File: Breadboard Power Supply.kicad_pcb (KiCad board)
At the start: 2 copper layers, 53.6 x 25.8 mm, 25 parts, among them J1 USB-C, J10 Conn_01x02_Male, J11 Conn_01x02_Male, J2 Conn_02x03_Odd_Even, J3 Conn_02x03_Odd_Even, J8 Conn_01x02_Male, J9 Conn_01x02_Male, U1 LM1117-1.8, U2 LM1117-3.3

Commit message: Layout tweaks.
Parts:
- moved R3 6.83 mm to (115.7, 75.9)
- moved R2 5.83 mm to (140.0, 76.2), turned to 0 degrees
- moved R1 1.63 mm to (136.9, 76.2), turned to 0 degrees
- moved C3 1.62 mm to (144.8, 80.6), turned to 90 degrees
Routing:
- net Net-(D1-K): track 5.49 -> 0.00 mm
- net Net-(J1-CC1): track 7.59 -> 12.9 mm
- net GND: track 23.8 -> 22.3 mm, vias 11 -> 6
- net Net-(J1-CC2): track 9.84 -> 11.2 mm
- net +3.3V: track 66.1 -> 65.6 mm
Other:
- board text added: "5"
- board text removed: "4"

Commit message: Layout tweaks.
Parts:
- moved C1 4.44 mm to (142.9, 80.6), turned to 90 degrees
- moved C6 1.78 mm to (111.8, 81.3)
- moved C8 1.20 mm to (112.1, 78.2), turned to 0 degrees
- moved C3 0.76 mm to (144.8, 79.9)
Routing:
- net +3.3V: track 65.6 -> 55.1 mm
- net GND: track 22.3 -> 19.4 mm, vias 6 -> 11
- net +1V8: track 56.1 -> 58.4 mm

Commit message: Layout tweaks.
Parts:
- moved C6 1.45 mm to (112.6, 80.1), turned to 0 degrees
- moved R1 0.64 mm to (136.3, 76.2)
- moved R3 0.25 mm to (115.7, 76.2)
- moved U1 0.25 mm to (105.9, 81.2)
- moved R2 0.13 mm to (140.1, 76.2), turned to 180 degrees
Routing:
- net /BOTTOM_POWER_RAIL: track 0.00 -> 15.6 mm
- net /TOP_POWER_RAIL: track 0.00 -> 15.4 mm
- net +3.3V: track 55.1 -> 66.1 mm, vias 2 -> 4
- net Net-(D1-K): track 0.00 -> 3.14 mm
- net GND: track 19.4 -> 22.5 mm
- net Net-(J1-CC1): track 12.9 -> 14.7 mm
- net +1V8: track 58.4 -> 57.7 mm

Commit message: Completed layout.
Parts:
- moved TP2 2.54 mm to (118.1, 83.1)
- moved TP3 2.54 mm to (138.4, 83.1)
- moved C3 1.78 mm to (144.9, 81.7)
- moved R1 0.76 mm to (137.0, 76.2)
- moved C1 0.28 mm to (143.0, 80.9)
- moved U2 0.25 mm to (150.6, 81.2)
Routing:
- net Net-(J1-CC1): track 14.7 -> 17.0 mm
- net GND: track 22.5 -> 24.7 mm
- net +1V8: track 57.7 -> 56.3 mm, vias 0 -> 1
- net +5V: track 78.6 -> 77.3 mm
- net Net-(J1-CC2): track 11.0 -> 11.9 mm
- net +3.3V: track 66.1 -> 66.0 mm, vias 4 -> 2
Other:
- outline, holes or cut-outs redrawn

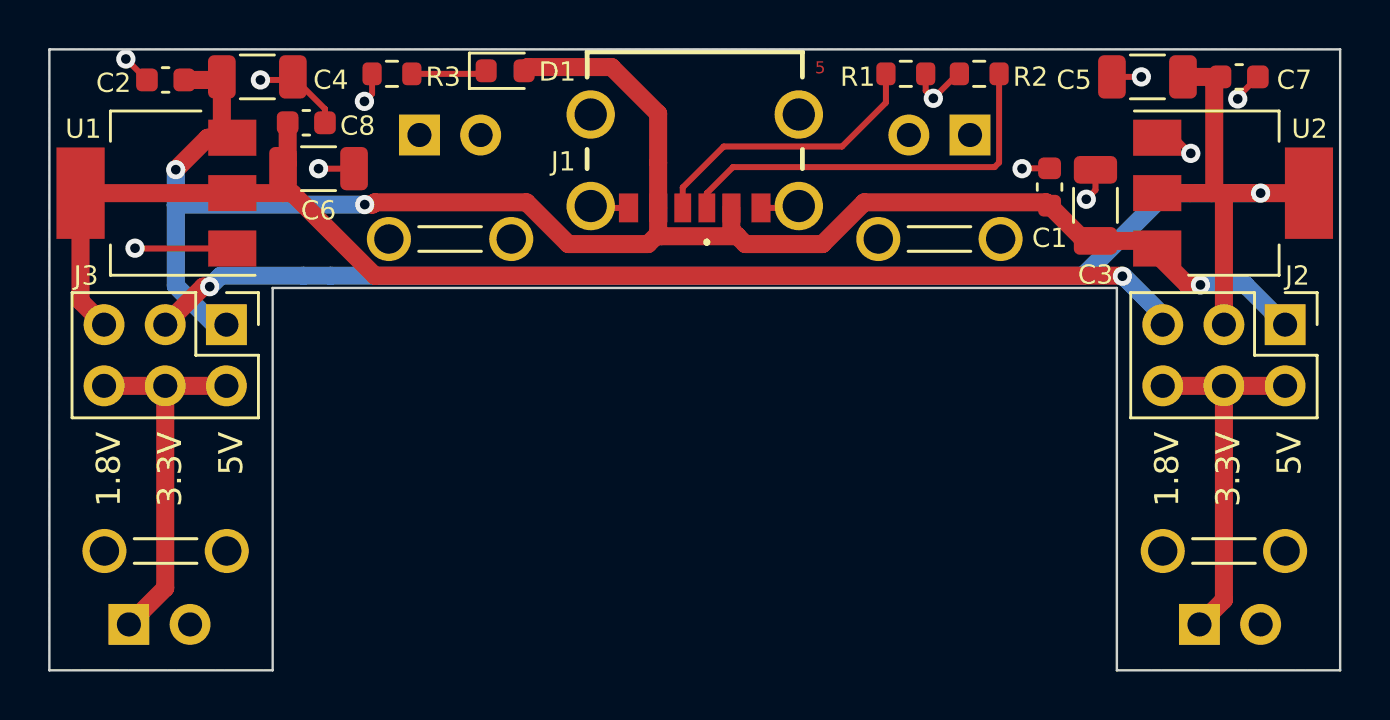
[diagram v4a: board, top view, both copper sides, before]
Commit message: Replaced 10uF footprints with 0805.
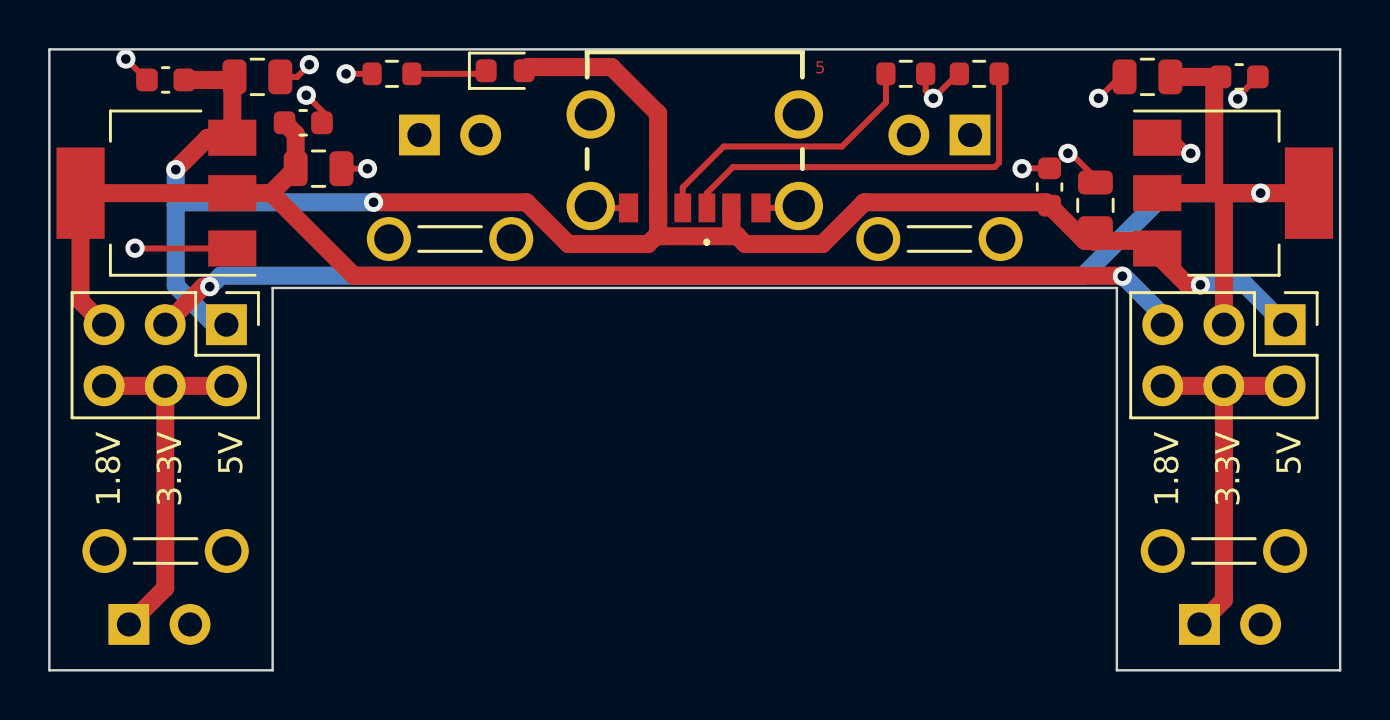
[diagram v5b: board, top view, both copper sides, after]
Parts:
- C3, C4, C5, C6: footprint Capacitor_SMD:C_1206_3216Metric -> Capacitor_SMD:C_0805_2012Metric
- R3: value 470 -> 1k
- moved C8 0.13 mm to (112.0, 78.2)
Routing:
- net GND: track 24.7 -> 23.8 mm, vias 11 -> 12
- net +1V8: track 56.3 -> 56.8 mm

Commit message: Release candidate.
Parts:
- moved C7 7.55 mm to (143.4, 77.3), turned to 90 degrees
- moved C2 6.89 mm to (113.2, 77.1), turned to 90 degrees
- moved J8 5.08 mm to (149.2, 94.0)
- moved J9 5.08 mm to (104.8, 94.0)
- moved J2 2.29 mm to (152.8, 84.3)
- moved J3 2.29 mm to (108.8, 84.3)
- moved U1 2.29 mm to (105.9, 78.9)
- moved U2 2.29 mm to (150.6, 78.9)
- moved C8 2.22 mm to (113.2, 80.1), turned to -90 degrees
- moved C5 2.03 mm to (145.2, 77.0), turned to 90 degrees
- moved R3 1.66 mm to (117.3, 76.1)
- moved C4 1.42 mm to (111.4, 77.0), turned to 90 degrees
- moved C6 1.30 mm to (111.4, 80.4), turned to -90 degrees
- moved C3 1.23 mm to (145.2, 80.5)
- moved TP1 1.02 mm to (106.3, 97.0)
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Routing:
- net +1V8: track 56.8 -> 92.3 mm, vias 1 -> 2
- net GND: track 23.8 -> 30.4 mm, vias 12 -> 8
- net +5V: track 77.2 -> 71.2 mm, vias 3 -> 1
- net /BOTTOM_POWER_RAIL: track 15.6 -> 12.8 mm
- net /TOP_POWER_RAIL: track 15.4 -> 12.8 mm, vias 0 -> 1
- net +3.3V: track 66.0 -> 64.2 mm, vias 2 -> 1
- net Net-(D1-K): track 3.14 -> 1.44 mm
- net Net-(J1-CC1): track 17.0 -> 16.3 mm
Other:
- board size 53.6 x 25.8 mm -> 53.6 x 23.2 mm

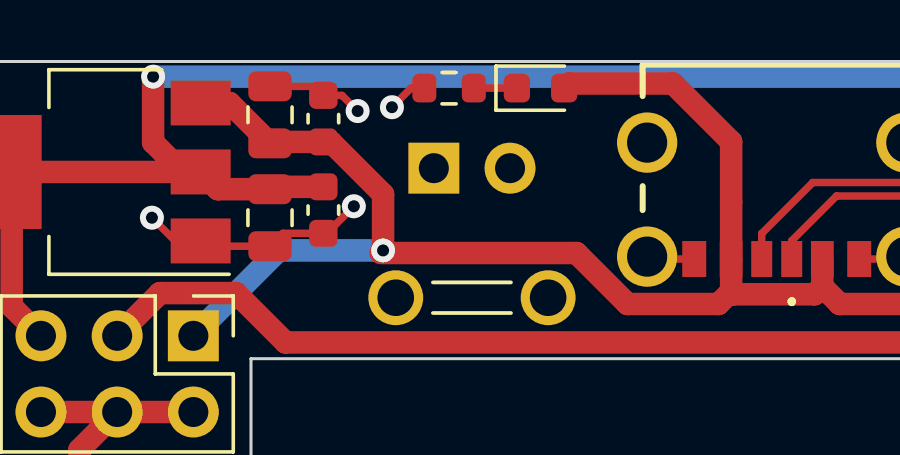
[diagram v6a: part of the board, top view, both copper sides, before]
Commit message: Added an 0402 resistor.
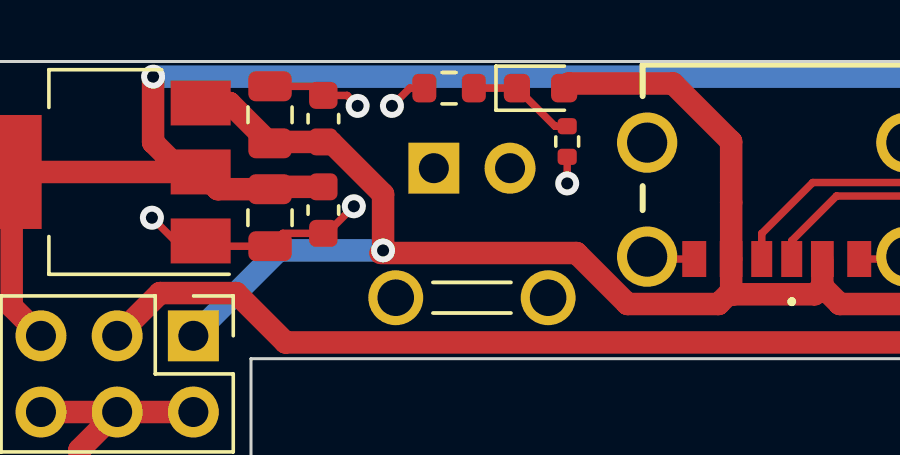
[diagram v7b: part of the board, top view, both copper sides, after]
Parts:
- added R4: 1k, Resistor_SMD:R_0402_1005Metric, F.Cu at (121.3, 77.9)
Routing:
- net Net-(D1-K): track 1.44 -> 3.64 mm
- net GND: track 30.4 -> 31.2 mm, vias 8 -> 9
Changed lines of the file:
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@@
       (net 1 "GND") (pinfunction "2") (pintype "passive"))
+  )
+  (footprint "Resistor_SMD:R_0402_1005Metric" (layer "F.Cu")
+    (at 121.285 77.851 -90)
+    (descr "Resistor SMD 0402 (1005 Metric), square (rectangular) end terminal, IPC_7351 nominal, (Body size source: IPC-SM-782 page 72, https://www.pcb-3d.com/wordpress/wp-content/uploads/ipc-sm-782a_amendment_1_and_2.pdf), generated with kicad-footprint-generator")
+    (tags "resistor")
+    (property "Digi-Key Part Num" "311-1.00KLRCT-ND")
+    (property "Sheetfile" "Breadboard Power Supply.kicad_sch")
+    (property "Sheetname" "")
+    (property "ki_description" "Resistor, US symbol")
+    (property "ki_keywords" "R res resistor")
+    (attr smd)
+    (fp_text reference "R4" (at 0 -1.17 90) (layer "F.SilkS") hide
+        (effects (font (size 1 1) (thickness 0.15)))
+    )
+    (fp_text value "1k" (at 0 1.17 90) (layer "F.Fab")
+        (effects (font (size 1 1) (thickness 0.15)))
+    )
+    (fp_text user "${REFERENCE}" (at 0 0 90) (layer "F.Fab")
+        (effects (font (size 0.26 0.26) (thickness 0.04)))
+    )
+    (fp_line (start -0.153641 -0.38) (end 0.153641 -0.38)
+      (stroke (width 0.12) (type solid)) (layer "F.SilkS"))
+    (fp_line (start -0.153641 0.38) (end 0.153641 0.38)
+      (stroke (width 0.12) (type solid)) (layer "F.SilkS"))
+    (fp_line (start -0.93 -0.47) (end 0.93 -0.47)
+      (stroke (width 0.05) (type solid)) (layer "F.CrtYd"))
+    (fp_line (start -0.93 0.47) (end -0.93 -0.47)
+      (stroke (width 0.05) (type solid)) (layer "F.CrtYd"))
+    (fp_line (start 0.93 -0.47) (end 0.93 0.47)
+      (stroke (width 0.05) (type solid)) (layer "F.CrtYd"))
+    (fp_line (start 0.93 0.47) (end -0.93 0.47)
+      (stroke (width 0.05) (type solid)) (layer "F.CrtYd"))
+    (fp_line (start -0.525 -0.27) (end 0.525 -0.27)
+      (stroke (width 0.1) (type solid)) (layer "F.Fab"))
+    (fp_line (start -0.525 0.27) (end -0.525 -0.27)
+      (stroke (width 0.1) (type solid)) (layer "F.Fab"))
+    (fp_line (start 0.525 -0.27) (end 0.525 0.27)
+      (stroke (width 0.1) (type solid)) (layer "F.Fab"))
+    (fp_line (start 0.525 0.27) (end -0.525 0.27)
+      (stroke (width 0.1) (type solid)) (layer "F.Fab"))
+    (pad "1" smd roundrect (at -0.51 0 270) (size 0.54 0.64) (layers "F.Cu" "F.Paste" "F.Mask") (roundrect_rratio 0.25)
+      (net 5 "Net-(D1-K)") (pintype "passive"))
+    (pad "2" smd roundrect (at 0.51 0 270) (size 0.54 0.64) (layers "F.Cu" "F.Paste" "F.Mask") (roundrect_rratio 0.25)
+      (net 1 "GND") (pintype "passive"))
+    (model "${KICAD6_3DMODEL_DIR}/Resistor_SMD.3dshapes/R_0402_1005Metric.wrl"
+      (offset (xyz 0 0 0))
+      (scale (xyz 1 1 1))
+      (rotate (xyz 0 0 0))
+    )
   )
   (footprint "Package_TO_SOT_SMD:SOT-223-3_TabPin2" (layer "F.Cu")
@@
   (segment (start 143.383 79.809) (end 142.293 79.809) (width 0.25) (layer "F.Cu") (net 1))
   (segment (start 113.157 80.912) (end 113.271 80.912) (width 0.25) (layer "F.Cu") (net 1))
+  (segment (start 113.949852 76.314) (end 113.157 76.314) (width 0.25) (layer "F.Cu") (net 1))
   (segment (start 147.8995 76.567) (end 147.472 76.567) (width 0.25) (layer "F.Cu") (net 1))
   (segment (start 137.858 76.898) (end 138.176 77.216) (width 0.25) (layer "F.Cu") (net 1))
   (segment (start 113.271 80.912) (end 114.173 80.01) (width 0.25) (layer "F.Cu") (net 1))
+  (segment (start 121.285 78.361) (end 121.285 79.248) (width 0.25) (layer "F.Cu") (net 1))
   (segment (start 142.293 79.809) (end 142.24 79.756) (width 0.25) (layer "F.Cu") (net 1))
   (segment (start 142.010022 76.507) (end 143.383 76.507) (width 0.25) (layer "F.Cu") (net 1))
-  (segment (start 113.779 76.314) (end 113.157 76.314) (width 0.25) (layer "F.Cu") (net 1))
+  (segment (start 114.3 76.664148) (end 113.949852 76.314) (width 0.25) (layer "F.Cu") (net 1))
   (segment (start 132.51 81.768) (end 132.59 81.688) (width 0.25) (layer "F.Cu") (net 1))
   (segment (start 145.161 76.078) (end 145.65 76.567) (width 0.25) (layer "F.Cu") (net 1))
   (segment (start 124.03 81.768) (end 123.95 81.688) (width 0.25) (layer "F.Cu") (net 1))
   (segment (start 131.02 81.768) (end 132.51 81.768) (width 0.25) (layer "F.Cu") (net 1))
-  (segment (start 114.3 76.835) (end 113.779 76.314) (width 0.25) (layer "F.Cu") (net 1))
   (segment (start 111.379 76.012) (end 112.855 76.012) (width 0.25) (layer "F.Cu") (net 1))
   (segment (start 143.685 79.507) (end 143.383 79.809) (width 0.25) (layer "F.Cu") (net 1))
+  (segment (start 116.034148 76.073) (end 116.523 76.073) (width 0.25) (layer "F.Cu") (net 1))
   (segment (start 137.858 76.2) (end 137.858 76.898) (width 0.25) (layer "F.Cu") (net 1))
   (segment (start 145.65 76.567) (end 147.472 76.567) (width 0.25) (layer "F.Cu") (net 1))
@@
   (segment (start 125.52 81.768) (end 124.03 81.768) (width 0.25) (layer "F.Cu") (net 1))
   (segment (start 111.808 80.912) (end 111.379 81.341) (width 0.25) (layer "F.Cu") (net 1))
-  (segment (start 115.443 76.708) (end 116.078 76.073) (width 0.25) (layer "F.Cu") (net 1))
   (segment (start 112.855 76.012) (end 113.157 76.314) (width 0.25) (layer "F.Cu") (net 1))
-  (segment (start 116.078 76.073) (end 116.523 76.073) (width 0.25) (layer "F.Cu") (net 1))
   (segment (start 149.225 77.8925) (end 147.8995 76.567) (width 0.25) (layer "F.Cu") (net 1))
+  (segment (start 115.443 76.664148) (end 116.034148 76.073) (width 0.25) (layer "F.Cu") (net 1))
   (segment (start 111.379 81.341) (end 109.242 81.341) (width 0.25) (layer "F.Cu") (net 1))
   (segment (start 109.242 81.341) (end 109.068 81.167) (width 0.25) (layer "F.Cu") (net 1))
   (segment (start 141.256889 77.260133) (end 142.010022 76.507) (width 0.25) (layer "F.Cu") (net 1))
   (via (at 138.176 77.216) (size 0.8) (drill 0.4) (layers "F.Cu" "B.Cu") (net 1))
-  (via (at 115.443 76.708) (size 0.8) (drill 0.4) (layers "F.Cu" "B.Cu") (net 1))
+  (via (at 115.443 76.664148) (size 0.8) (drill 0.4) (layers "F.Cu" "B.Cu") (net 1))
   (via (at 142.24 79.756) (size 0.8) (drill 0.4) (layers "F.Cu" "B.Cu") (net 1))
-  (via (at 114.3 76.835) (size 0.8) (drill 0.4) (layers "F.Cu" "B.Cu") (net 1))
+  (via (at 114.3 76.664148) (size 0.8) (drill 0.4) (layers "F.Cu" "B.Cu") (net 1))
+  (via (at 121.285 79.248) (size 0.8) (drill 0.4) (layers "F.Cu" "B.Cu") (net 1))
   (via (at 114.173 80.01) (size 0.8) (drill 0.4) (layers "F.Cu" "B.Cu") (net 1))
   (via (at 149.225 77.8925) (size 0.8) (drill 0.4) (layers "F.Cu" "B.Cu") (net 1))
@@
   (segment (start 106.284 86.868) (end 108.824 86.868) (width 0.75) (layer "F.Cu") (net 4))
   (segment (start 105.029 93.726) (end 105.029 88.123) (width 0.75) (layer "F.Cu") (net 4))
+  (segment (start 120.8765 77.341) (end 119.6085 76.073) (width 0.25) (layer "F.Cu") (net 5))
+  (segment (start 121.285 77.341) (end 120.8765 77.341) (width 0.25) (layer "F.Cu") (net 5))
   (segment (start 118.173 76.073) (end 119.6085 76.073) (width 0.25) (layer "F.Cu") (net 5))
   (segment (start 137.440538 75.4) (end 136.933 75.907538) (width 0.25) (layer "F.Cu") (net 6))

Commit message: Implemented most items in Feedback.
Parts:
- removed R3: 1k, Resistor_SMD:R_0603_1608Metric
- added D2: SMBJ5.0A-TR, My-Global-Footprints:SMB_STM, B.Cu at (128.3, 79.9)
- C1, C2, C7, C8: footprint Capacitor_SMD:C_0603_1608Metric -> Capacitor_SMD:C_0402_1005Metric
- R1, R2: footprint Resistor_SMD:R_0603_1608Metric -> Resistor_SMD:R_0402_1005Metric
- moved R4 3.86 mm to (117.9, 76.1), turned to 180 degrees
- moved R2 1.14 mm to (138.9, 76.2), turned to 0 degrees
- moved C1 0.87 mm to (143.6, 79.8)
- moved C2 0.68 mm to (112.9, 77.7)
- moved C7 0.62 mm to (143.6, 77.9)
- moved C8 0.59 mm to (112.9, 79.6)
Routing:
- net GND: track 31.2 -> 21.5 mm, vias 9 -> 11
- net Net-(J1-CC1): track 16.3 -> 12.9 mm
- net Net-(D1-K): track 3.64 -> 1.24 mm
- net +5V: track 71.2 -> 70.5 mm
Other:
- board text added: "6"
- board text removed: "5"
